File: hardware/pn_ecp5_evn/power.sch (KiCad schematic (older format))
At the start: 33 parts, among them U501 LM27761, U502 ADM7171ACPZ-3.3-R7, U503 TPS72301DB

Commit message: first pass footprint assignment on pn r0
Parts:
- added C513, C514: 100 uF, Capacitor_SMD:C_0402_1005Metric, symbol Device:C_Small
- added D503: B3L30LP, vna:AP02002_DFN8_DIODE, symbol Device:D_Small
- added D504: 5.1V, Diode_SMD:D_SOD-323, symbol Device:D_Zener_Small
- added L502: BLM15GG471, Inductor_SMD:L_0402_1005Metric, symbol Device:L_Small
- added L503: 1 uH, LPWI252010S1R0T, Inductor_SMD:L_1008_2520Metric, symbol Device:L_Small
- C501, C505, C507, C512: value 4.7 uF -> 10 uF; footprint (none) -> Capacitor_SMD:C_0603_1608Metric
- C502, C508: value C_Small -> 1 uF; footprint (none) -> Capacitor_SMD:C_0402_1005Metric
- C503, C510: footprint (none) -> Capacitor_SMD:C_0402_1005Metric
- C504, C509, C511: value C_Small -> 10 uF; footprint (none) -> Capacitor_SMD:C_0603_1608Metric
- C506: value C_Small -> 1 nF; footprint (none) -> Capacitor_SMD:C_0402_1005Metric
- D501, D502: value LED_Small -> RED; footprint (none) -> LED_SMD:LED_0603_1608Metric
- L501: value L_Small -> BLM15GG471; footprint (none) -> Inductor_SMD:L_0402_1005Metric
- R501: value R_Small -> 0; footprint (none) -> Resistor_SMD:R_0402_1005Metric
- R502, R506: footprint (none) -> Resistor_SMD:R_0402_1005Metric
- R503: value R_Small -> DNI; footprint (none) -> Resistor_SMD:R_0402_1005Metric
- R504: value TBD -> 88.7k; footprint (none) -> Resistor_SMD:R_0402_1005Metric
- R505: value TBD -> 49.9k; footprint (none) -> Resistor_SMD:R_0402_1005Metric
- R507, R508: value R_Small -> 10k; footprint (none) -> Resistor_SMD:R_0402_1005Metric
- R509: value TBD -> 33k; footprint (none) -> Resistor_SMD:R_0402_1005Metric
- R510: value TBD -> 64.9k; footprint (none) -> Resistor_SMD:R_0402_1005Metric
- TP501, TP502, TP503, TP504, TP505: footprint (none) -> TestPoint:TestPoint_Keystone_5015_Micro-Minature
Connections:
- net -1V8: now also L502.2; no longer C512.1, R509.1, TP505.1, U503.5 (OUT)
- net -3V3: now also U503.3 (EN)
- net GND: now also C513.2, C514.2, D504.2 (A)
- net VPP: now also C513.1, C514.1, L503.2
- new net: C512.1, L502.1, R509.1, TP505.1, U503.5 (OUT)
- new net: D503.1 (K), D504.1 (K), L503.1
- new net VIN: D503.2 (A)
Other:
- note added: ""Driving EN over 1.5 V or below –1.5 V turns on the regulator.""
- note added: "Vout = -1.186 * (1 + Rout_fb / Rfb_gnd)\nRout_fb + Rfb_gnd = 100k"
- note added: "Vout = -1.22 * ((Rout_fb + Rfb_gnd) / Rfb_gnd)\nRfb_gnd > 50k\n"
- note removed: "Vout = -1.186 * (Rout_fb / Rfb_gnd)\nRout_fb + Rfb_gnd ~= 100k"
- note removed: "Vout = -1.2 * ((Rout_fb + Rfb_gnd) / Rfb_gnd)\nRfb_gnd > 50k\n"

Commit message: started component placement on phase noise analyzer
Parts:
- removed TP501: TestPoint, TestPoint:TestPoint_Keystone_5015_Micro-Minature, symbol Connector:TestPoint
- C513, C514: value 100 uF -> 270 uF; footprint Capacitor_SMD:C_0402_1005Metric -> Capacitor_SMD:CP_Elec_6.3x5.9; symbol Device:C_Small -> Device:CP_Small; MPN (none) -> 875105245014
- U503: footprint TO_SOT_Packages_SMD:SOT-23-5 -> Package_TO_SOT_SMD:SOT-23-5
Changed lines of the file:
@@
-	1    0    0    -1
-$EndComp
-$Comp
-L Connector:TestPoint TP501
-U 1 1 5F2686E1
-P 3950 1300
-F 0 "TP501" H 4008 1418 50  0000 L CNN
-F 1 "TestPoint" H 4008 1327 50  0000 L CNN
-F 2 "TestPoint:TestPoint_Keystone_5015_Micro-Minature" H 4150 1300 50  0001 C CNN
-F 3 "~" H 4150 1300 50  0001 C CNN
-	1    3950 1300
-	1    0    0    -1
-$EndComp
-$Comp
-L Connector:TestPoint TP?
-U 1 1 5F74588A
-P 4900 1300
-AR Path="/5F4ECD93/5F74588A" Ref="TP?"  Part="1"
-AR Path="/5F2678A0/5F74588A" Ref="TP502"  Part="1"
-F 0 "TP502" H 4958 1418 50  0000 L CNN
-F 1 "TestPoint" H 4958 1327 50  0000 L CNN
-F 2 "TestPoint:TestPoint_Keystone_5015_Micro-Minature" H 5100 1300 50  0001 C CNN
-F 3 "~" H 5100 1300 50  0001 C CNN
-	1    4900 1300
 	1    0    0    -1
 $EndComp
@@
 $EndComp
 Connection ~ 3950 1450
-Wire Wire Line
-	4900 1300 4900 1450
-Connection ~ 4900 1450
-Wire Wire Line
-	3950 1300 3950 1450
 $Comp
 L Connector:TestPoint TP504
@@
 F 0 "U503" H 8450 4865 50  0000 C CNN
 F 1 "TPS72301DB" H 8450 4774 50  0000 C CNN
-F 2 "TO_SOT_Packages_SMD:SOT-23-5" H 8450 5000 50  0001 C CNN
+F 2 "Package_TO_SOT_SMD:SOT-23-5" H 8450 5000 50  0001 C CNN
 F 3 "http://www.ti.com/lit/ds/symlink/tps723.pdf" H 8450 4600 50  0001 C CNN
 	1    8450 4500
@@
 	1700 1850 1700 2050
 $Comp
-L Device:C_Small C513
-U 1 1 5F4FA838
-P 2550 1750
-F 0 "C513" H 2642 1796 50  0000 L CNN
-F 1 "100 uF" H 2642 1705 50  0000 L CNN
-F 2 "Capacitor_SMD:C_0402_1005Metric" H 2550 1750 50  0001 C CNN
-F 3 "~" H 2550 1750 50  0001 C CNN
-	1    2550 1750
-	1    0    0    -1
-$EndComp
-$Comp
-L power:GND #PWR0283
-U 1 1 5F4FAD3F
-P 2550 2050
-F 0 "#PWR0283" H 2550 1800 50  0001 C CNN
-F 1 "GND" H 2555 1877 50  0000 C CNN
-F 2 "" H 2550 2050 50  0001 C CNN
-F 3 "" H 2550 2050 50  0001 C CNN
-	1    2550 2050
-	1    0    0    -1
-$EndComp
-Wire Wire Line
-	2550 2050 2550 1850
-$Comp
-L Device:C_Small C514
+L Device:CP_Small C514
 U 1 1 5F4FEB95
 P 3050 1750
 F 0 "C514" H 3142 1796 50  0000 L CNN
-F 1 "100 uF" H 3142 1705 50  0000 L CNN
-F 2 "Capacitor_SMD:C_0402_1005Metric" H 3050 1750 50  0001 C CNN
+F 1 "270 uF" H 3142 1705 50  0000 L CNN
+F 2 "Capacitor_SMD:CP_Elec_6.3x5.9" H 3050 1750 50  0001 C CNN
 F 3 "~" H 3050 1750 50  0001 C CNN
+F 4 "875105245014" H 3050 1750 50  0001 C CNN "MPN"
 	1    3050 1750
 	1    0    0    -1
@@
 Wire Wire Line
 	3050 1850 3050 2050
-Wire Wire Line
-	2000 1450 2550 1450
-Wire Wire Line
-	2550 1650 2550 1450
-Connection ~ 2550 1450
-Wire Wire Line
-	2550 1450 3050 1450
 Wire Wire Line
 	3050 1650 3050 1450
@@
 	0    1    1    0
 $EndComp
+Connection ~ 4900 1450
+Wire Wire Line
+	4900 1300 4900 1450
+$Comp
+L Connector:TestPoint TP?
+U 1 1 5F74588A
+P 4900 1300
+AR Path="/5F4ECD93/5F74588A" Ref="TP?"  Part="1"
+AR Path="/5F2678A0/5F74588A" Ref="TP502"  Part="1"
+F 0 "TP502" H 4958 1418 50  0000 L CNN
+F 1 "TestPoint" H 4958 1327 50  0000 L CNN
+F 2 "TestPoint:TestPoint_Keystone_5015_Micro-Minature" H 5100 1300 50  0001 C CNN
+F 3 "~" H 5100 1300 50  0001 C CNN
+	1    4900 1300
+	1    0    0    -1
+$EndComp
+Wire Wire Line
+	2550 1450 3050 1450
+Wire Wire Line
+	2000 1450 2550 1450
+Connection ~ 2550 1450
+Wire Wire Line
+	2550 1650 2550 1450
+Wire Wire Line
+	2550 2050 2550 1850
+$Comp
+L power:GND #PWR0283
+U 1 1 5F4FAD3F
+P 2550 2050
+F 0 "#PWR0283" H 2550 1800 50  0001 C CNN
+F 1 "GND" H 2555 1877 50  0000 C CNN
+F 2 "" H 2550 2050 50  0001 C CNN
+F 3 "" H 2550 2050 50  0001 C CNN
+	1    2550 2050
+	1    0    0    -1
+$EndComp
+$Comp
+L Device:CP_Small C513
+U 1 1 5F4FA838
+P 2550 1750
+F 0 "C513" H 2642 1796 50  0000 L CNN
+F 1 "270 uF" H 2642 1705 50  0000 L CNN
+F 2 "Capacitor_SMD:CP_Elec_6.3x5.9" H 2550 1750 50  0001 C CNN
+F 3 "~" H 2550 1750 50  0001 C CNN
+F 4 "875105245014" H 2550 1750 50  0001 C CNN "MPN"
+	1    2550 1750
+	1    0    0    -1
+$EndComp
 $EndSCHEMATC

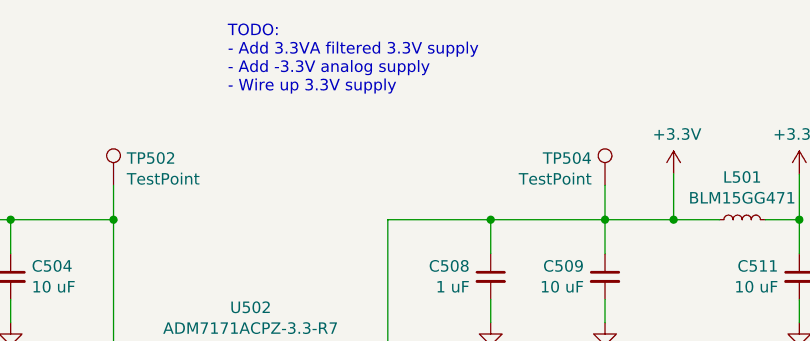
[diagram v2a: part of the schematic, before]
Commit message: final layout cleanup, ordered phase noise downconverter boards
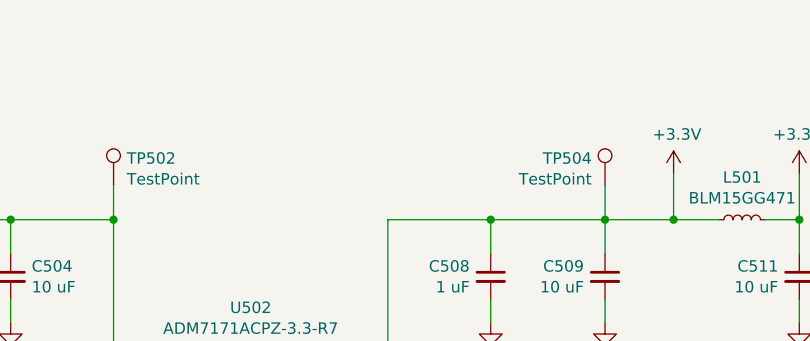
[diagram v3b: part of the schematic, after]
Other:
- note removed: "TODO:\n- Add 3.3VA filtered 3.3V supply\n- Add -3.3V analog supply\n- Wire up 3.3V supply"
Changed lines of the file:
@@
 	1    0    0    -1
 $EndComp
-Text Notes 5400 900  0    50   ~ 0
-TODO:\n- Add 3.3VA filtered 3.3V supply\n- Add -3.3V analog supply\n- Wire up 3.3V supply
 $Comp
 L Regulator_SwitchedCapacitor:LM27761 U501

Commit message: added part numbers to schematic of phase noise downconverter, ordered
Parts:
- C501, C502, C503, C504, C505, C506, C507, C508, C509, C510, C511, C512, D501, D502, R503, R504, R505, R507, R508, R509, R510: Distributor Part Number (none) -> N/A
- C513, C514: Distributor (none) -> Digi-Key; Distributor Part Number (none) -> 732-6414-1-ND
- D503: Distributor (none) -> Digi-Key; Distributor Part Number (none) -> B3L30LP-7DICT-ND
- D504: Distributor (none) -> Digi-Key; Distributor Part Number (none) -> MM3Z5V1ST1GOSCT-ND
- L501, L502: Distributor (none) -> Digi-Key; Distributor Part Number (none) -> 490-5198-1-ND
- L503: Distributor (none) -> Digi-Key; Distributor Part Number (none) -> F10235CT-ND
- R501, R502, R506: Distributor (none) -> Digi-Key; Distributor Part Number (none) -> P0.0JCT-ND
- TP502, TP503, TP504, TP505: Distributor (none) -> Digi-Key; Distributor Part Number (none) -> 36-5015CT-ND
- U501: Distributor (none) -> Digi-Key; Distributor Part Number (none) -> 296-44379-1-ND
- U502: Distributor (none) -> Digi-Key; Distributor Part Number (none) -> ADM7171ACPZ-3.3-R7CT-ND
- U503: Distributor (none) -> Digi-Key; Distributor Part Number (none) -> TPS72301DBVR
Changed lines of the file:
@@
 F 2 "Package_DFN_QFN:DFN-8-1EP_3x3mm_P0.5mm_EP1.66x2.38mm" H 5350 2750 50  0001 C CNN
 F 3 "https://www.analog.com/media/en/technical-documentation/data-sheets/ADM7170.pdf" H 5450 2550 50  0001 C CNN
+F 4 "Digi-Key" H 5500 2250 50  0001 C CNN "Distributor"
+F 5 "ADM7171ACPZ-3.3-R7CT-ND" H 5500 2250 50  0001 C CNN "Distributor Part Number"
 	1    5500 2250
 	1    0    0    -1
@@
 F 2 "Package_SON:WSON-8-1EP_2x2mm_P0.5mm_EP0.9x1.6mm" H 4850 4200 50  0001 L CNN
 F 3 "http://www.ti.com/lit/ds/symlink/lm27761.pdf" H 7200 4300 50  0001 C CNN
+F 4 "Digi-Key" H 4700 4700 50  0001 C CNN "Distributor"
+F 5 "296-44379-1-ND" H 4700 4700 50  0001 C CNN "Distributor Part Number"
 	1    4700 4700
 	1    0    0    -1
@@
 F 2 "Resistor_SMD:R_0402_1005Metric" H 4650 2800 50  0001 C CNN
 F 3 "~" H 4650 2800 50  0001 C CNN
+F 4 "N/A" H 4650 2800 50  0001 C CNN "Distributor Part Number"
 	1    4650 2800
 	1    0    0    -1
@@
 F 2 "Resistor_SMD:R_0402_1005Metric" H 3950 2550 50  0001 C CNN
 F 3 "~" H 3950 2550 50  0001 C CNN
+F 4 "Digi-Key" H 3950 2550 50  0001 C CNN "Distributor"
+F 5 "P0.0JCT-ND " H 3950 2550 50  0001 C CNN "Distributor Part Number"
 	1    3950 2550
 	0    1    1    0
@@
 F 2 "Capacitor_SMD:C_0603_1608Metric" H 4450 1700 50  0001 C CNN
 F 3 "~" H 4450 1700 50  0001 C CNN
+F 4 "N/A" H 4450 1700 50  0001 C CNN "Distributor Part Number"
 	1    4450 1700
 	1    0    0    -1
@@
 F 2 "Capacitor_SMD:C_0402_1005Metric" H 3950 1700 50  0001 C CNN
 F 3 "~" H 3950 1700 50  0001 C CNN
+F 4 "N/A" H 3950 1700 50  0001 C CNN "Distributor Part Number"
 	1    3950 1700
 	1    0    0    -1
@@
 F 2 "TestPoint:TestPoint_Keystone_5015_Micro-Minature" H 7250 1300 50  0001 C CNN
 F 3 "~" H 7250 1300 50  0001 C CNN
+F 4 "Digi-Key" H 7050 1300 50  0001 C CNN "Distributor"
+F 5 "36-5015CT-ND" H 7050 1300 50  0001 C CNN "Distributor Part Number"
 	1    7050 1300
 	-1   0    0    -1
@@
 F 2 "Capacitor_SMD:C_0402_1005Metric" H 6550 1700 50  0001 C CNN
 F 3 "~" H 6550 1700 50  0001 C CNN
+F 4 "N/A" H 6550 1700 50  0001 C CNN "Distributor Part Number"
 	1    6550 1700
 	-1   0    0    -1
@@
 F 2 "Capacitor_SMD:C_0603_1608Metric" H 7050 1700 50  0001 C CNN
 F 3 "~" H 7050 1700 50  0001 C CNN
+F 4 "N/A" H 7050 1700 50  0001 C CNN "Distributor Part Number"
 	1    7050 1700
 	-1   0    0    -1
@@
 F 2 "Inductor_SMD:L_0402_1005Metric" H 7650 1450 50  0001 C CNN
 F 3 "~" H 7650 1450 50  0001 C CNN
+F 4 "Digi-Key" H 7650 1450 50  0001 C CNN "Distributor"
+F 5 "490-5198-1-ND" H 7650 1450 50  0001 C CNN "Distributor Part Number"
 	1    7650 1450
 	0    -1   -1   0
@@
 F 2 "Capacitor_SMD:C_0603_1608Metric" H 7900 1700 50  0001 C CNN
 F 3 "~" H 7900 1700 50  0001 C CNN
+F 4 "N/A" H 7900 1700 50  0001 C CNN "Distributor Part Number"
 	1    7900 1700
 	-1   0    0    -1
@@
 F 2 "Capacitor_SMD:C_0402_1005Metric" H 6100 2850 50  0001 C CNN
 F 3 "~" H 6100 2850 50  0001 C CNN
+F 4 "N/A" H 6100 2850 50  0001 C CNN "Distributor Part Number"
 	1    6100 2850
 	-1   0    0    -1
@@
 F 2 "Capacitor_SMD:C_0402_1005Metric" H 4100 4850 50  0001 C CNN
 F 3 "~" H 4100 4850 50  0001 C CNN
+F 4 "N/A" H 4100 4850 50  0001 C CNN "Distributor Part Number"
 	1    4100 4850
 	-1   0    0    -1
@@
 F 2 "TestPoint:TestPoint_Keystone_5015_Micro-Minature" H 6000 4150 50  0001 C CNN
 F 3 "~" H 6000 4150 50  0001 C CNN
+F 4 "Digi-Key" H 5800 4150 50  0001 C CNN "Distributor"
+F 5 "36-5015CT-ND" H 5800 4150 50  0001 C CNN "Distributor Part Number"
 	1    5800 4150
 	-1   0    0    -1
@@
 F 2 "LED_SMD:LED_0603_1608Metric" V 8900 1600 50  0001 C CNN
 F 3 "~" V 8900 1600 50  0001 C CNN
+F 4 "N/A" H 8900 1600 50  0001 C CNN "Distributor Part Number"
 	1    8900 1600
 	0    -1   -1   0
@@
 F 2 "Resistor_SMD:R_0402_1005Metric" H 8900 2000 50  0001 C CNN
 F 3 "~" H 8900 2000 50  0001 C CNN
+F 4 "N/A" H 8900 2000 50  0001 C CNN "Distributor Part Number"
 	1    8900 2000
 	1    0    0    -1
@@
 F 2 "LED_SMD:LED_0603_1608Metric" V 9550 1600 50  0001 C CNN
 F 3 "~" V 9550 1600 50  0001 C CNN
+F 4 "N/A" H 9550 1600 50  0001 C CNN "Distributor Part Number"
 	1    9550 1600
 	0    1    1    0
@@
 F 2 "Resistor_SMD:R_0402_1005Metric" H 9550 2000 50  0001 C CNN
 F 3 "~" H 9550 2000 50  0001 C CNN
+F 4 "N/A" H 9550 2000 50  0001 C CNN "Distributor Part Number"
 	1    9550 2000
 	1    0    0    -1
@@
 F 2 "Package_TO_SOT_SMD:SOT-23-5" H 8450 5000 50  0001 C CNN
 F 3 "http://www.ti.com/lit/ds/symlink/tps723.pdf" H 8450 4600 50  0001 C CNN
+F 4 "Digi-Key" H 8450 4500 50  0001 C CNN "Distributor"
+F 5 "TPS72301DBVR" H 8450 4500 50  0001 C CNN "Distributor Part Number"
 	1    8450 4500
 	1    0    0    -1
@@
 F 2 "Resistor_SMD:R_0402_1005Metric" H 4000 4300 50  0001 C CNN
 F 3 "~" H 4000 4300 50  0001 C CNN
+F 4 "Digi-Key" H 4000 4300 50  0001 C CNN "Distributor"
+F 5 "P0.0JCT-ND " H 4000 4300 50  0001 C CNN "Distributor Part Number"
 	1    4000 4300
 	1    0    0    -1
@@
 F 2 "Capacitor_SMD:C_0603_1608Metric" H 5500 5100 50  0001 C CNN
 F 3 "~" H 5500 5100 50  0001 C CNN
+F 4 "N/A" H 5500 5100 50  0001 C CNN "Distributor Part Number"
 	1    5500 5100
 	-1   0    0    -1
@@
 F 2 "Resistor_SMD:R_0402_1005Metric" H 5800 4500 50  0001 C CNN
 F 3 "~" H 5800 4500 50  0001 C CNN
+F 4 "N/A" H 5800 4500 50  0001 C CNN "Distributor Part Number"
 	1    5800 4500
 	1    0    0    -1
@@
 F 2 "Resistor_SMD:R_0402_1005Metric" H 5800 4850 50  0001 C CNN
 F 3 "~" H 5800 4850 50  0001 C CNN
+F 4 "N/A" H 5800 4850 50  0001 C CNN "Distributor Part Number"
 	1    5800 4850
 	1    0    0    -1
@@
 F 2 "Capacitor_SMD:C_0603_1608Metric" H 6200 4850 50  0001 C CNN
 F 3 "~" H 6200 4850 50  0001 C CNN
+F 4 "N/A" H 6200 4850 50  0001 C CNN "Distributor Part Number"
 	1    6200 4850
 	-1   0    0    -1
@@
 F 2 "Resistor_SMD:R_0402_1005Metric" H 6450 4400 50  0001 C CNN
 F 3 "~" H 6450 4400 50  0001 C CNN
+F 4 "Digi-Key" H 6450 4400 50  0001 C CNN "Distributor"
+F 5 "P0.0JCT-ND " H 6450 4400 50  0001 C CNN "Distributor Part Number"
 	1    6450 4400
 	0    1    1    0
@@
 F 2 "Capacitor_SMD:C_0603_1608Metric" H 3600 4850 50  0001 C CNN
 F 3 "~" H 3600 4850 50  0001 C CNN
+F 4 "N/A" H 3600 4850 50  0001 C CNN "Distributor Part Number"
 	1    3600 4850
 	-1   0    0    -1
@@
 F 2 "Capacitor_SMD:C_0402_1005Metric" H 7700 4850 50  0001 C CNN
 F 3 "~" H 7700 4850 50  0001 C CNN
+F 4 "N/A" H 7700 4850 50  0001 C CNN "Distributor Part Number"
 	1    7700 4850
 	-1   0    0    -1
@@
 F 2 "Capacitor_SMD:C_0603_1608Metric" H 10100 4800 50  0001 C CNN
 F 3 "~" H 10100 4800 50  0001 C CNN
+F 4 "N/A" H 10100 4800 50  0001 C CNN "Distributor Part Number"
 	1    10100 4800
 	-1   0    0    -1
@@
 F 2 "Resistor_SMD:R_0402_1005Metric" H 9600 4550 50  0001 C CNN
 F 3 "~" H 9600 4550 50  0001 C CNN
+F 4 "N/A" H 9600 4550 50  0001 C CNN "Distributor Part Number"
 	1    9600 4550
 	1    0    0    -1
@@
 F 2 "Resistor_SMD:R_0402_1005Metric" H 9600 4950 50  0001 C CNN
 F 3 "~" H 9600 4950 50  0001 C CNN
+F 4 "N/A" H 9600 4950 50  0001 C CNN "Distributor Part Number"
 	1    9600 4950
 	1    0    0    -1
@@
 F 2 "TestPoint:TestPoint_Keystone_5015_Micro-Minature" H 10300 4250 50  0001 C CNN
 F 3 "~" H 10300 4250 50  0001 C CNN
+F 4 "Digi-Key" H 10100 4250 50  0001 C CNN "Distributor"
+F 5 "36-5015CT-ND" H 10100 4250 50  0001 C CNN "Distributor Part Number"
 	1    10100 4250
 	-1   0    0    -1
@@
 F 2 "Inductor_SMD:L_0402_1005Metric" H 10400 4400 50  0001 C CNN
 F 3 "~" H 10400 4400 50  0001 C CNN
+F 4 "Digi-Key" H 10400 4400 50  0001 C CNN "Distributor"
+F 5 "490-5198-1-ND" H 10400 4400 50  0001 C CNN "Distributor Part Number"
 	1    10400 4400
 	0    -1   -1   0
@@
 F 2 "vna:AP02002_DFN8_DIODE" V 1500 1450 50  0001 C CNN
 F 3 "~" V 1500 1450 50  0001 C CNN
+F 4 "B3L30LP-7DICT-ND" H 1500 1450 50  0001 C CNN "Distributor Part Number"
+F 5 "Digi-Key" H 1500 1450 50  0001 C CNN "Distributor"
 	1    1500 1450
 	-1   0    0    1
@@
 F 2 "Inductor_SMD:L_1008_2520Metric" H 1900 1450 50  0001 C CNN
 F 3 "~" H 1900 1450 50  0001 C CNN
+F 4 "Digi-Key" H 1900 1450 50  0001 C CNN "Distributor"
+F 5 "F10235CT-ND " H 1900 1450 50  0001 C CNN "Distributor Part Number"
 	1    1900 1450
 	0    -1   -1   0
@@
 F 3 "~" H 3050 1750 50  0001 C CNN
 F 4 "875105245014" H 3050 1750 50  0001 C CNN "MPN"
+F 5 "Digi-Key" H 3050 1750 50  0001 C CNN "Distributor"
+F 6 "732-6414-1-ND" H 3050 1750 50  0001 C CNN "Distributor Part Number"
 	1    3050 1750
 	1    0    0    -1
@@
 F 2 "Diode_SMD:D_SOD-323" V 1700 1750 50  0001 C CNN
 F 3 "~" V 1700 1750 50  0001 C CNN
+F 4 "MM3Z5V1ST1GOSCT-ND" H 1700 1750 50  0001 C CNN "Distributor Part Number"
+F 5 "Digi-Key" H 1700 1750 50  0001 C CNN "Distributor"
 	1    1700 1750
 	0    1    1    0
@@
 F 2 "TestPoint:TestPoint_Keystone_5015_Micro-Minature" H 5100 1300 50  0001 C CNN
 F 3 "~" H 5100 1300 50  0001 C CNN
+F 4 "Digi-Key" H 4900 1300 50  0001 C CNN "Distributor"
+F 5 "36-5015CT-ND" H 4900 1300 50  0001 C CNN "Distributor Part Number"
 	1    4900 1300
 	1    0    0    -1
@@
 F 3 "~" H 2550 1750 50  0001 C CNN
 F 4 "875105245014" H 2550 1750 50  0001 C CNN "MPN"
+F 5 "Digi-Key" H 2550 1750 50  0001 C CNN "Distributor"
+F 6 "732-6414-1-ND" H 2550 1750 50  0001 C CNN "Distributor Part Number"
 	1    2550 1750
 	1    0    0    -1
